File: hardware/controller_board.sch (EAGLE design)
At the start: 25 parts, among them J1 FRSKY-GIMBAL, J12 JST_3PIN_GND_VDD_SIG, J14 JST_3PIN_GND_VDD_SIG, J16 JST_3PIN_GND_VDD_SIG, J18 JST_3PIN_GND_VDD_SIG, J2 FRSKY-GIMBAL, J3 WIRE-HARNESS-SPARKFUN-9915

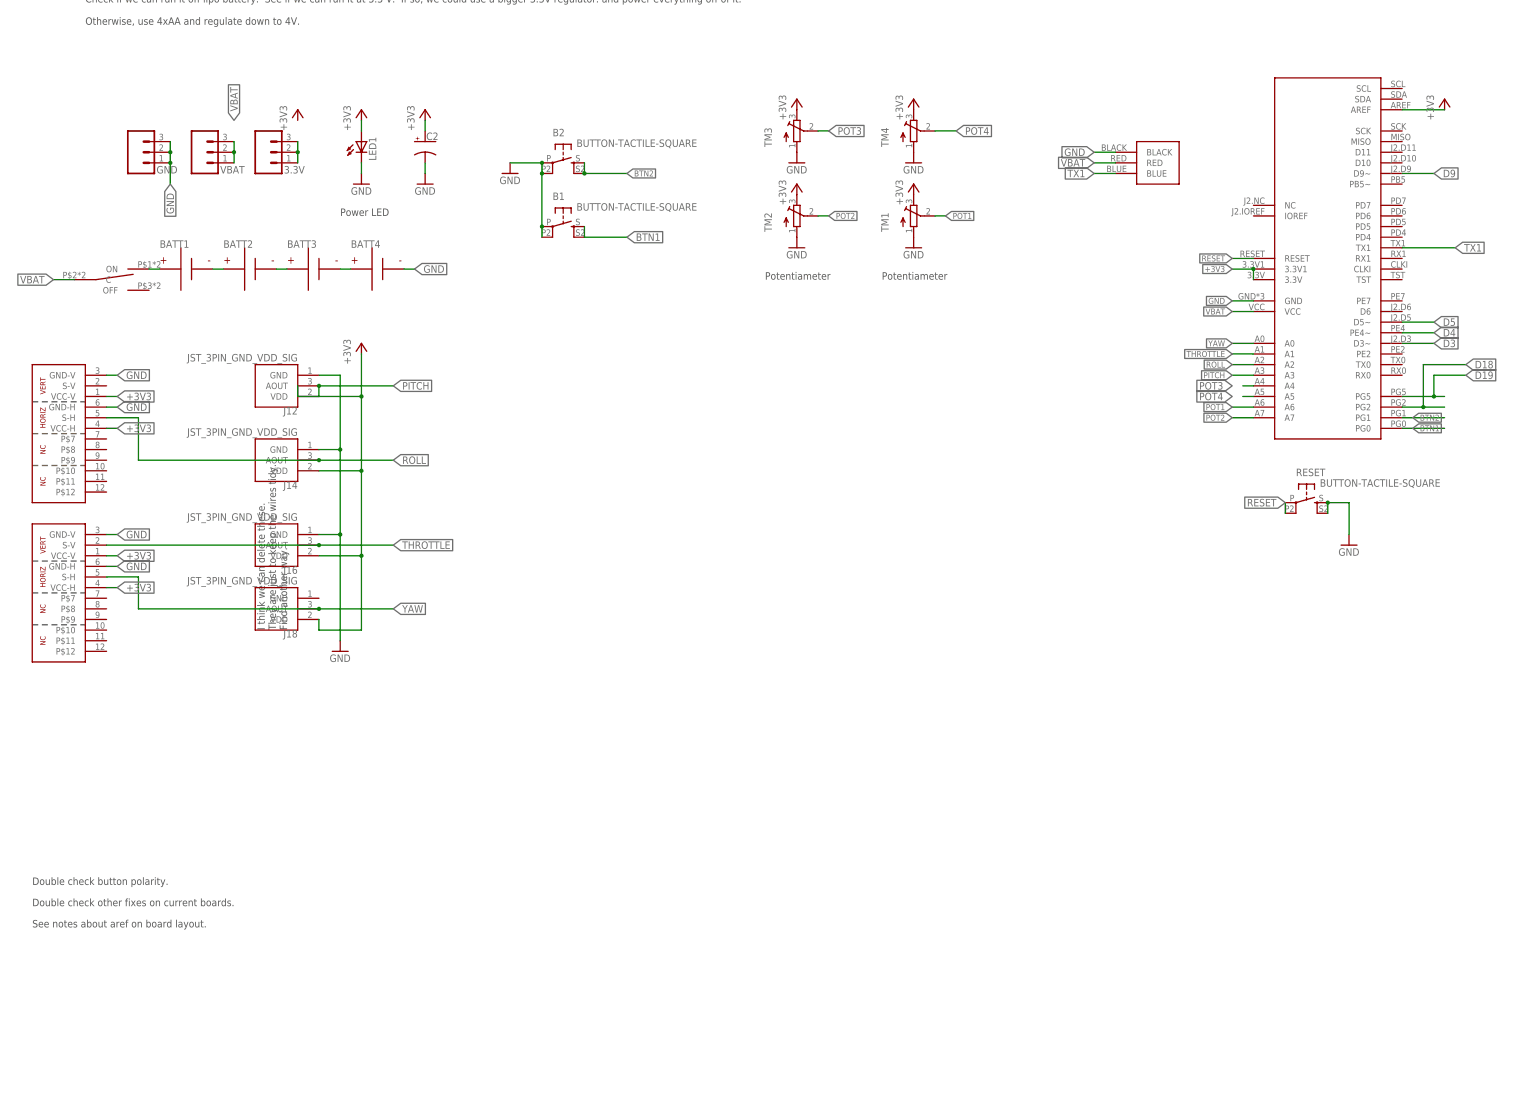
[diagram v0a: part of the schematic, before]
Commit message: import a bunch of components from quad schematic.  remove arduino breakout
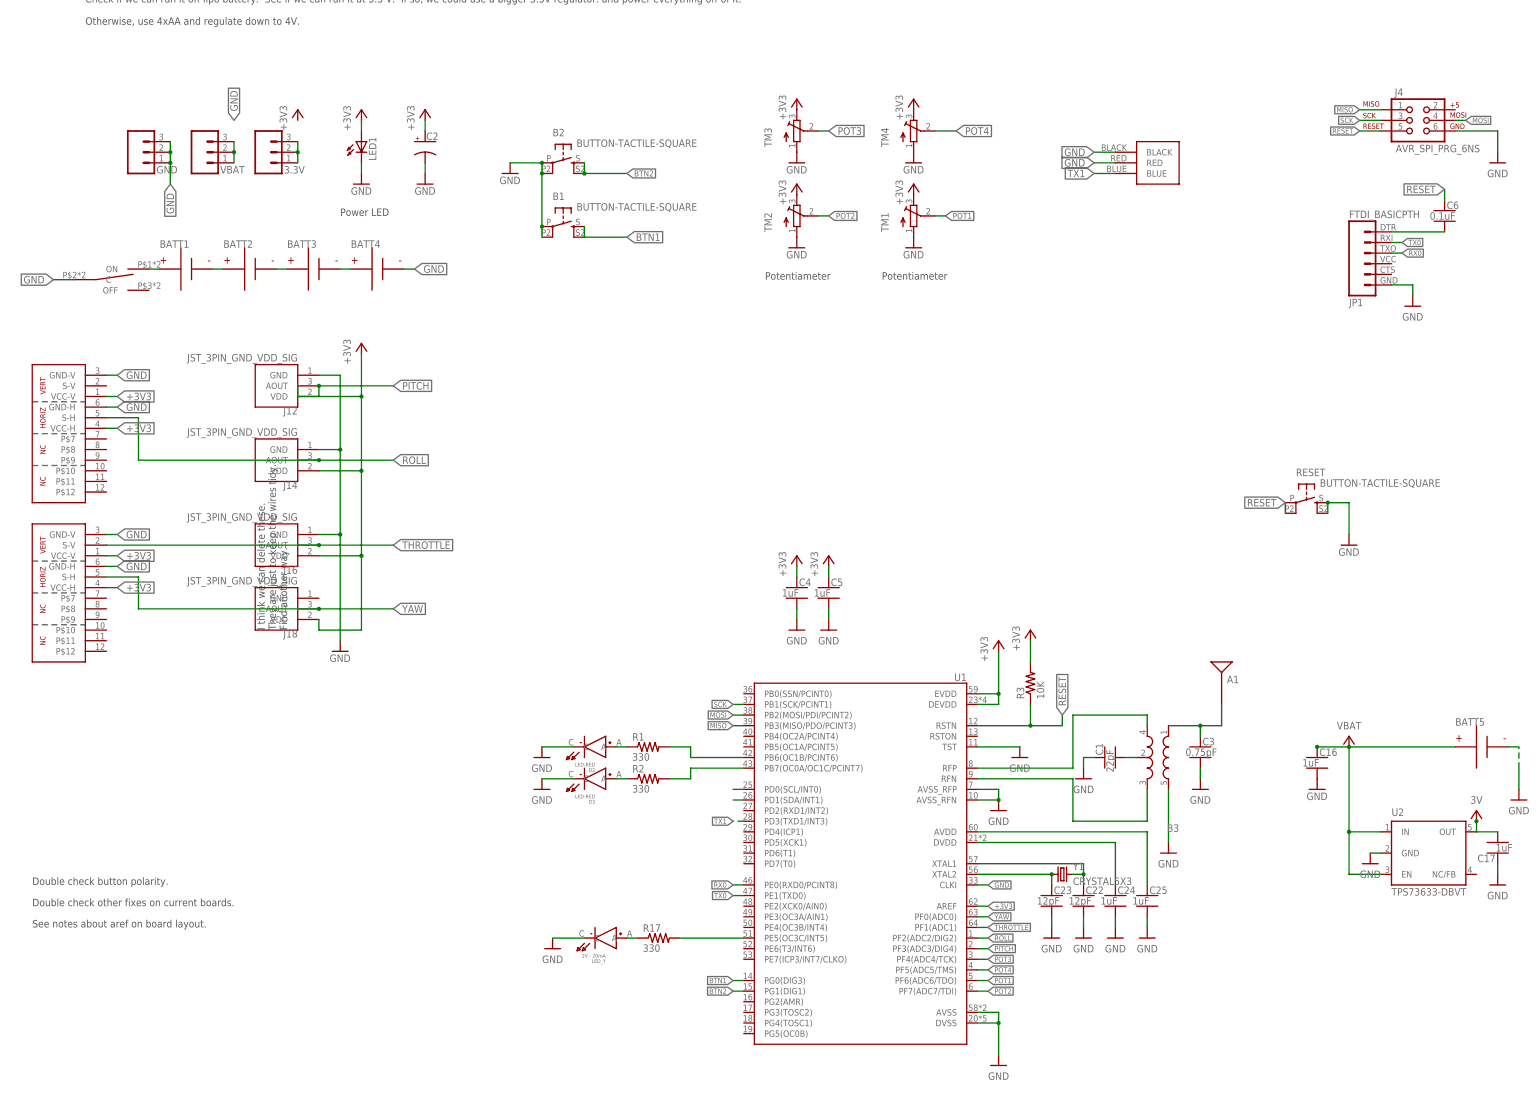
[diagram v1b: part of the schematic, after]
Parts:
- removed U$4: ATMEGA128RFA1-BOB, BOBs:ATMEGA128RFA1-BOB
- added A1: ANTENNA2SMD5, quadparts_prebuilt:ANTENNA2SMD5
- added B3: BALUN0805, quadparts_prebuilt:BALUN0805
- added BATT5: BATTERY-HUBSAN-W/HOLDER, quadparts_prebuilt:BATTERY-HUBSAN-W/HOLDER
- added C1: 22pF, quadparts_prebuilt:CAPACITOR-NP_SMD-2012-0805_CERAMIC-22PF
- added C16, C17, C24, C25, C4, C5: 1uF, quadparts_prebuilt:CAPACITOR-NP_SMD-2012-0805_CERAMIC-1UF
- added C22, C23: 12pF, quadparts_prebuilt:CAPACITOR-NP_SMD-2012-0805_CERAMIC-12PF
- added C3: 0.75pF, quadparts_prebuilt:CAPACITOR-NP_SMD-2012-0805_CERAMIC-0.75PF
- added C6: 0.1uF, quadparts_prebuilt:CAPACITOR-NP_SMD-2012-0805_CERAMIC-0.1UF
- added D2, D3: LED-RED, custom:LED-RED
- added J4: AVR_SPI_PRG_6NS, quadparts_prebuilt:AVR_SPI_PRG_6NS
- added JP1: FTDI_BASICPTH, quadparts_prebuilt:FTDI_BASICPTH
- added LED_Y: 2V - 20mA, custom:LEDCMD17
- added R1, R17, R2: 330, quadparts_prebuilt:RESISTOR_SMD-2012-0805-330
- added R3: 10K, quadparts_prebuilt:RESISTOR_SMD-2012-0805-10K
- added U1: ATMEGA128RFA1, quadparts_prebuilt:ATMEGA128RFA1
- added U2: TPS73633-DBVT, quadparts_prebuilt:TPS73633-DBVT
- added Y1: CRYSTAL5X3, quadparts_prebuilt:CRYSTAL5X3
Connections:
- removed net D18: U$4.PG2
- removed net D19: U$4.PG5
- removed net D3: U$4.D3~
- removed net D4: U$4.PE4~
- removed net D5: U$4.D5~
- removed net D9: U$4.D9~
- removed net VBAT: J3.RED, S1.C, U$4.VCC, VBAT.1, VBAT.2, VBAT.3
- new net 3V: C17.2, U2.OUT
- new net ANTENNA: A1.SIGNAL, B3.IN, C3.1
- new net MISO: J4.1, U1.PB3(MISO/PDO/PCINT3)
- new net MOSI: J4.4, U1.PB2(MOSI/PDI/PCINT2)
- new net N$10: D3.A, R2.1
- new net N$11: C6.2, JP1.1
- new net N$15: C22.1, U1.XTAL1, Y1.2
- new net N$16: R17.2, U1.PE5(OC3C/INT5)
- new net N$18: LED_Y.A, R17.1
- new net N$19: C23.1, U1.XTAL2, Y1.1
- new net N$20: C24.1, U1.DVDD
- new net N$21: C25.1, U1.AVDD
- new net N$4: R2.2, U1.PB7(OC0A/OC1C/PCINT7)
- new net N$7: B3.GND@2, C1.2
- new net N$8: R1.2, U1.PB6(OC1B/PCINT6)
- new net N$9: D2.A, R1.1
- new net RFN: B3.OUT2, U1.RFN
- new net RFP: B3.OUT1, U1.RFP
- new net RX0: JP1.3, U1.PE0(RXD0/PCINT8)
- new net SCK: J4.3, U1.PB1(SCK/PCINT1)
- new net SCL: U1.PD0(SCL/INT0)
- new net SDA: U1.PD1(SDA/INT1)
- new net TX0: JP1.2, U1.PE1(TXD0)
- net +3V3: now also C4.1, C5.1, R3.2, U1.AREF, U1.DEVDD, U1.EVDD; no longer U$4.3.3V, U$4.3.3V1, U$4.AREF
- net BTN1: now also U1.PG0(DIG3); no longer U$4.PG0
- net BTN2: now also U1.PG1(DIG1); no longer U$4.PG1
- net GND: now also B3.GND@5, BATT5.N, BATT5.P, C1.1, C16.1, C16.2, C17.1, C22.2, C23.2, C24.2, C25.2, C3.2, C4.2, C5.2, D2.C, D3.C, J3.RED, J4.6, JP1.6, LED_Y.C, S1.C, U1.AVSS, U1.AVSS_RFN, U1.AVSS_RFP, U1.CLKI, U1.DVSS, U1.TST, U2.EN, U2.GND, U2.IN, VBAT.1, VBAT.2, VBAT.3; no longer U$4.GND
- net PITCH: now also U1.PF3(ADC3/DIG4); no longer U$4.A3
- net POT1: now also U1.PF6(ADC6/TDO); no longer U$4.A6
- net POT2: now also U1.PF7(ADC7/TDI); no longer U$4.A7
- net POT3: now also U1.PF4(ADC4/TCK); no longer U$4.A4
- net POT4: now also U1.PF5(ADC5/TMS); no longer U$4.A5
- net RESET: now also C6.1, J4.5, R3.1, U1.RSTN; no longer U$4.RESET
- net ROLL: now also U1.PF2(ADC2/DIG2); no longer U$4.A2
- net THROTTLE: now also U1.PF1(ADC1); no longer U$4.A1
- net TX1: now also U1.PD3(TXD1/INT3); no longer U$4.TX1
- net YAW: now also U1.PF0(ADC0); no longer U$4.A0

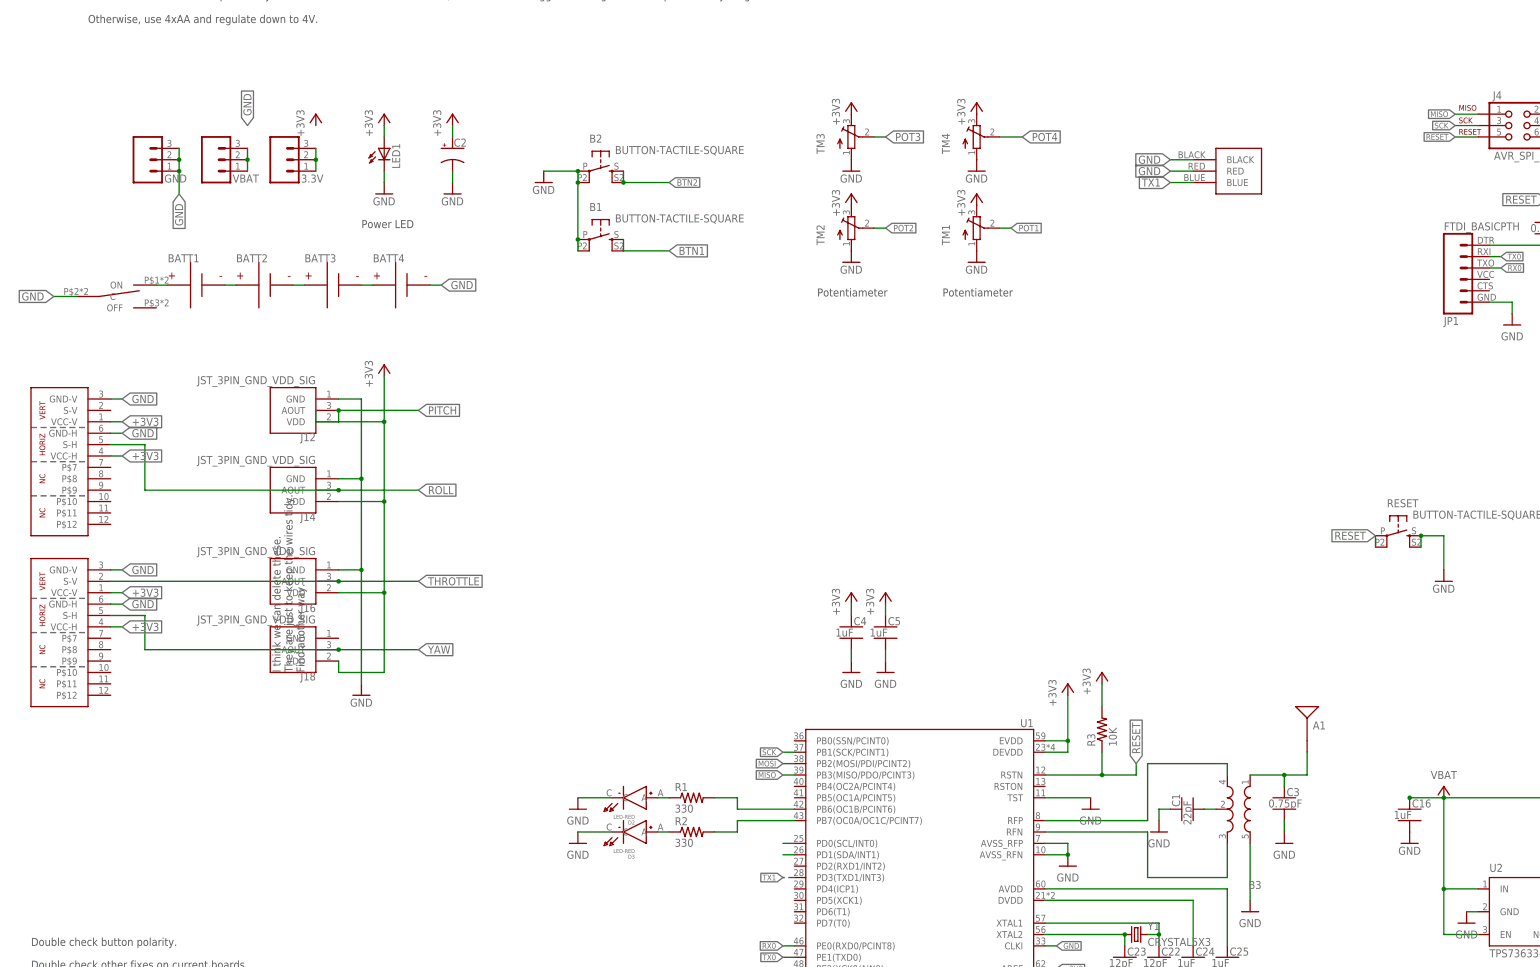
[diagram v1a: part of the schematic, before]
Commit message: cleanup and a few schematic fixes
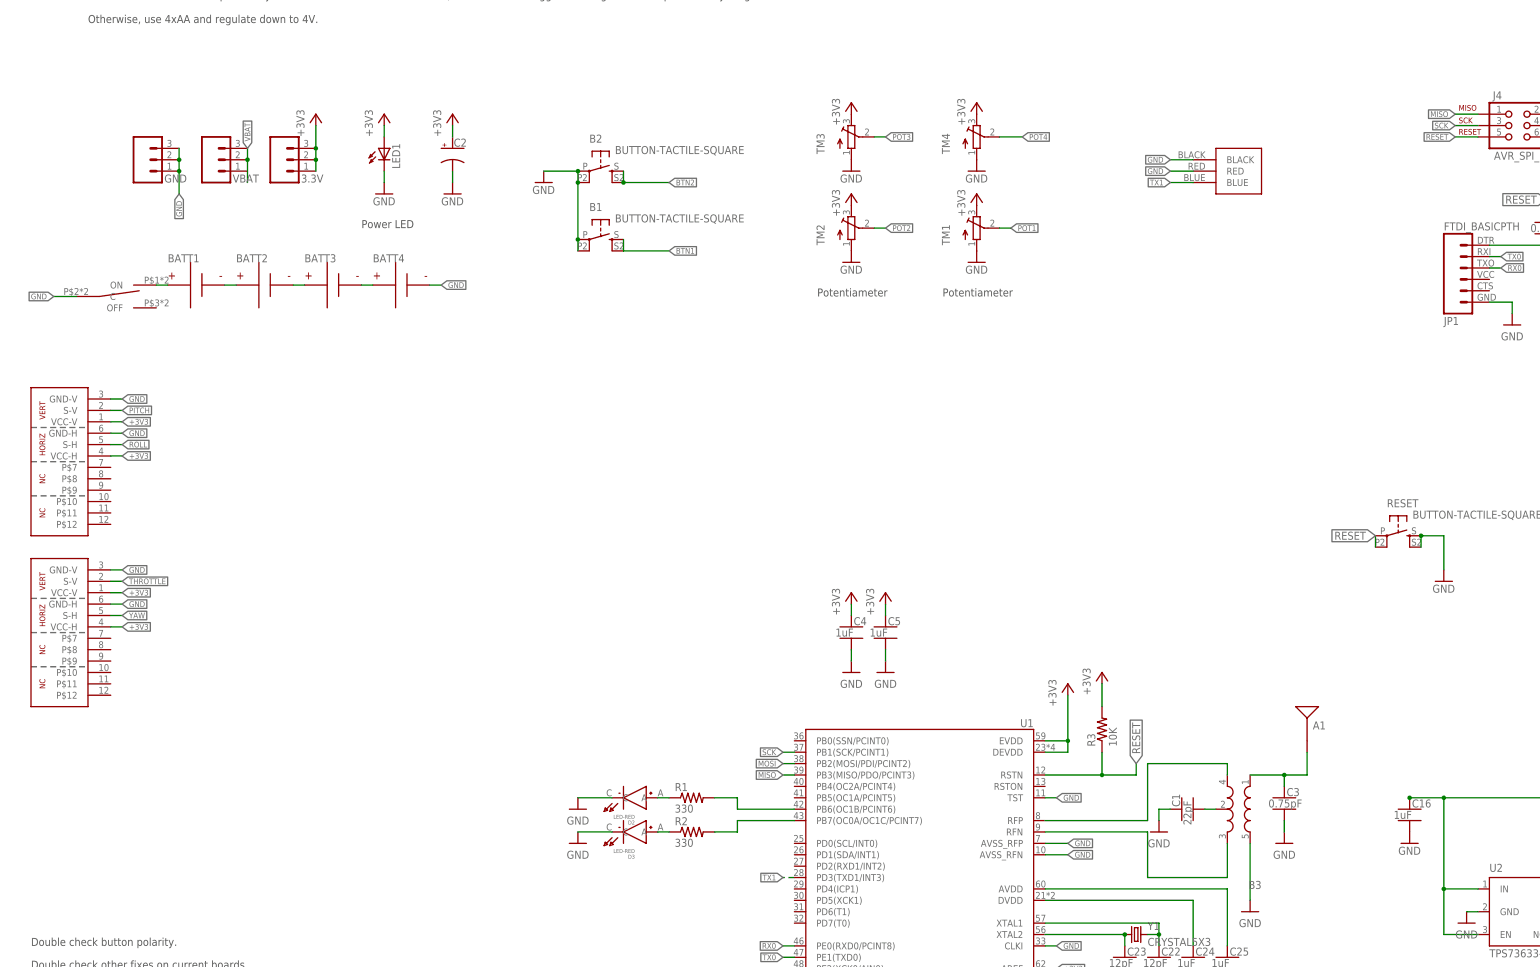
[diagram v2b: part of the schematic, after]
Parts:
- removed J12, J14, J16, J18: JST_3PIN_GND_VDD_SIG, RemoteParts:JST_3PIN_GND_VDD_SIG
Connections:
- removed net SCL: U1.PD0(SCL/INT0)
- removed net SDA: U1.PD1(SDA/INT1)
- new net VBAT: VBAT.2, VBAT.3
- net +3V3: now also 3.3V.1, 3.3V.2, 3.3V.3; no longer J12.VDD, J14.VDD, J16.VDD, J18.VDD
- net GND: no longer BATT5.P, C16.1, J12.GND, J14.GND, J16.GND, U2.EN, U2.IN, VBAT.1, VBAT.2, VBAT.3
- net N$6: now also BATT5.P, C16.1, U2.EN, U2.IN; no longer 3.3V.1, 3.3V.2, 3.3V.3
- net PITCH: now also J1.S-V; no longer J12.AOUT
- net ROLL: no longer J14.AOUT
- net THROTTLE: no longer J16.AOUT
- net YAW: no longer J18.AOUT
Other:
- note removed: "I think we can delete these. They are just to keep the wires tidy. Find another way."
